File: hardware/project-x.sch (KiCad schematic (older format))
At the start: 14 parts

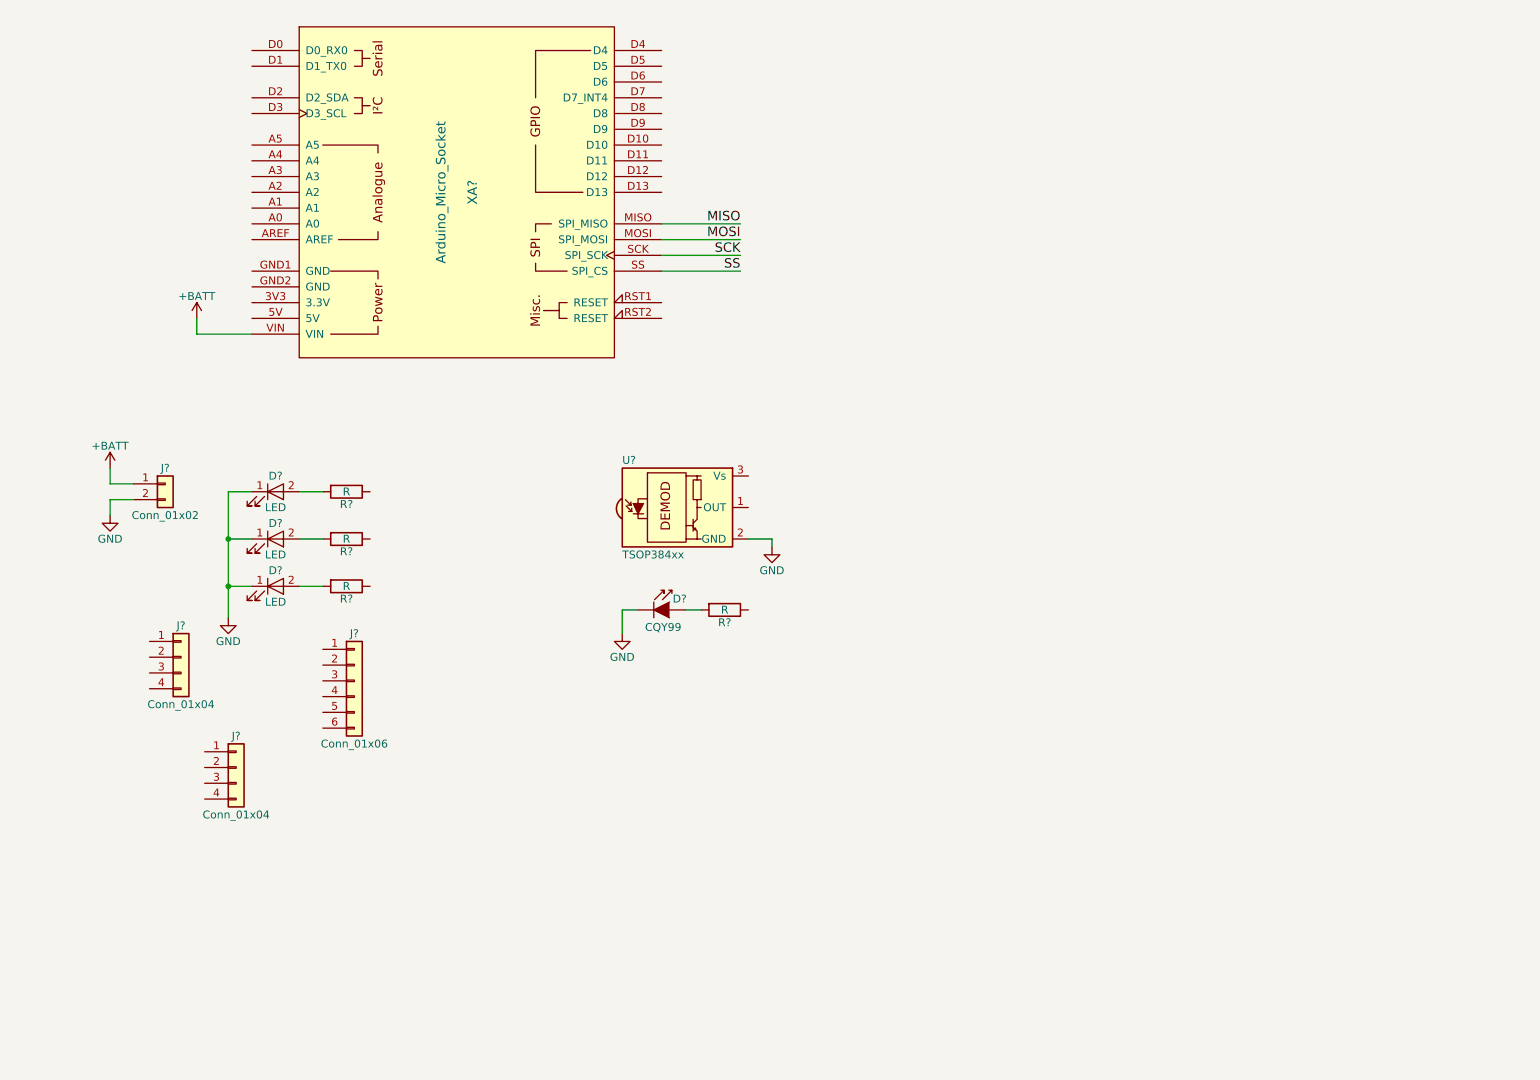
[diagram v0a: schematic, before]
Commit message: Add tags to schematic
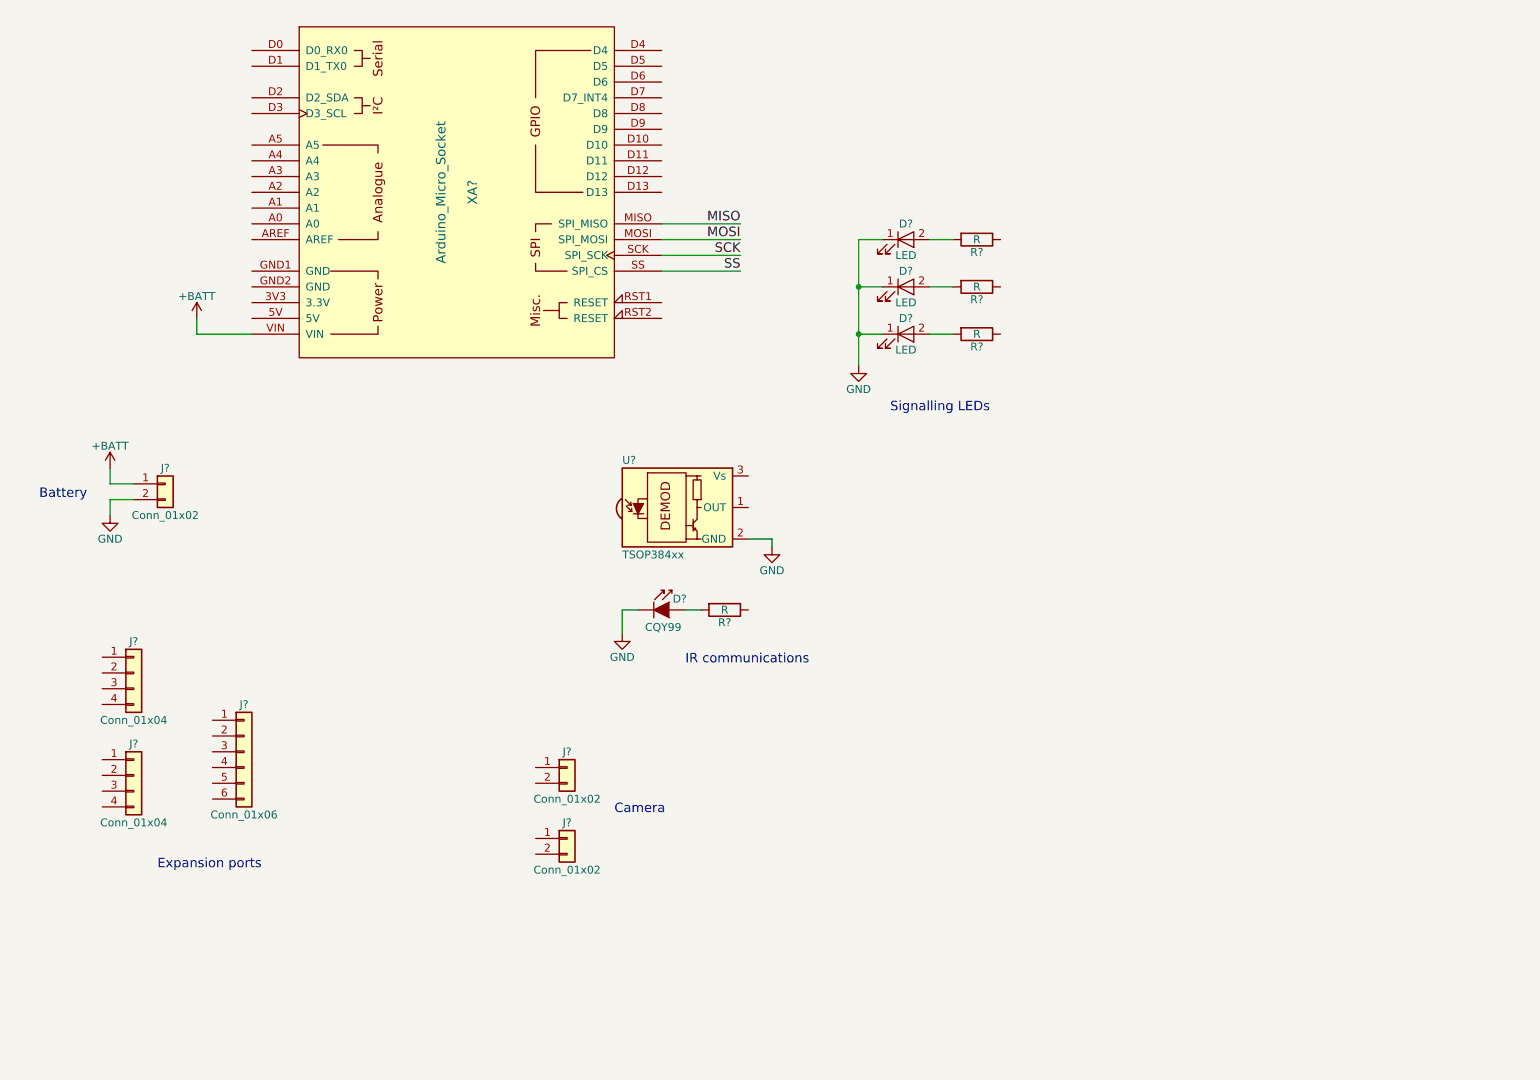
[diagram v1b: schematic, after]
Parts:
- added J? (x2): Conn_01x02, symbol Conn_01x02
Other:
- note added: "Battery"
- note added: "Camera"
- note added: "Expansion ports"
- note added: "IR communications"
- note added: "Signalling LEDs"
- moved on the sheet: D?, J?, R?
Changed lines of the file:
@@
 L LED D?
 U 1 1 5BD3A84D
-P 2200 4050
-F 0 "D?" H 2200 4150 50  0000 C CNN
-F 1 "LED" H 2200 3950 50  0000 C CNN
-F 2 "" H 2200 4050 50  0001 C CNN
-F 3 "" H 2200 4050 50  0001 C CNN
-	1    2200 4050
+P 6200 2450
+F 0 "D?" H 6200 2550 50  0000 C CNN
+F 1 "LED" H 6200 2350 50  0000 C CNN
+F 2 "" H 6200 2450 50  0001 C CNN
+F 3 "" H 6200 2450 50  0001 C CNN
+	1    6200 2450
 	1    0    0    -1
 $EndComp
@@
 L LED D?
 U 1 1 5BD3A889
-P 2200 4350
-F 0 "D?" H 2200 4450 50  0000 C CNN
-F 1 "LED" H 2200 4250 50  0000 C CNN
-F 2 "" H 2200 4350 50  0001 C CNN
-F 3 "" H 2200 4350 50  0001 C CNN
-	1    2200 4350
+P 6200 2750
+F 0 "D?" H 6200 2850 50  0000 C CNN
+F 1 "LED" H 6200 2650 50  0000 C CNN
+F 2 "" H 6200 2750 50  0001 C CNN
+F 3 "" H 6200 2750 50  0001 C CNN
+	1    6200 2750
 	1    0    0    -1
 $EndComp
@@
 L LED D?
 U 1 1 5BD3A8AF
-P 2200 4650
-F 0 "D?" H 2200 4750 50  0000 C CNN
-F 1 "LED" H 2200 4550 50  0000 C CNN
-F 2 "" H 2200 4650 50  0001 C CNN
-F 3 "" H 2200 4650 50  0001 C CNN
-	1    2200 4650
+P 6200 3050
+F 0 "D?" H 6200 3150 50  0000 C CNN
+F 1 "LED" H 6200 2950 50  0000 C CNN
+F 2 "" H 6200 3050 50  0001 C CNN
+F 3 "" H 6200 3050 50  0001 C CNN
+	1    6200 3050
 	1    0    0    -1
 $EndComp
@@
 L R R?
 U 1 1 5BD3A8D3
-P 2650 4050
-F 0 "R?" V 2730 4050 50  0000 C CNN
-F 1 "R" V 2650 4050 50  0000 C CNN
-F 2 "" V 2580 4050 50  0001 C CNN
-F 3 "" H 2650 4050 50  0001 C CNN
-	1    2650 4050
+P 6650 2450
+F 0 "R?" V 6730 2450 50  0000 C CNN
+F 1 "R" V 6650 2450 50  0000 C CNN
+F 2 "" V 6580 2450 50  0001 C CNN
+F 3 "" H 6650 2450 50  0001 C CNN
+	1    6650 2450
 	0    1    1    0
 $EndComp
@@
 L R R?
 U 1 1 5BD3A8F8
-P 2650 4350
-F 0 "R?" V 2730 4350 50  0000 C CNN
-F 1 "R" V 2650 4350 50  0000 C CNN
-F 2 "" V 2580 4350 50  0001 C CNN
-F 3 "" H 2650 4350 50  0001 C CNN
-	1    2650 4350
+P 6650 2750
+F 0 "R?" V 6730 2750 50  0000 C CNN
+F 1 "R" V 6650 2750 50  0000 C CNN
+F 2 "" V 6580 2750 50  0001 C CNN
+F 3 "" H 6650 2750 50  0001 C CNN
+	1    6650 2750
 	0    1    1    0
 $EndComp
@@
 L R R?
 U 1 1 5BD3A947
-P 2650 4650
-F 0 "R?" V 2730 4650 50  0000 C CNN
-F 1 "R" V 2650 4650 50  0000 C CNN
-F 2 "" V 2580 4650 50  0001 C CNN
-F 3 "" H 2650 4650 50  0001 C CNN
-	1    2650 4650
+P 6650 3050
+F 0 "R?" V 6730 3050 50  0000 C CNN
+F 1 "R" V 6650 3050 50  0000 C CNN
+F 2 "" V 6580 3050 50  0001 C CNN
+F 3 "" H 6650 3050 50  0001 C CNN
+	1    6650 3050
 	0    1    1    0
 $EndComp
@@
 L Conn_01x04 J?
 U 1 1 5BD3A97E
-P 1600 5100
-F 0 "J?" H 1600 5300 50  0000 C CNN
-F 1 "Conn_01x04" H 1600 4800 50  0000 C CNN
-F 2 "" H 1600 5100 50  0001 C CNN
-F 3 "" H 1600 5100 50  0001 C CNN
-	1    1600 5100
+P 1300 5200
+F 0 "J?" H 1300 5400 50  0000 C CNN
+F 1 "Conn_01x04" H 1300 4900 50  0000 C CNN
+F 2 "" H 1300 5200 50  0001 C CNN
+F 3 "" H 1300 5200 50  0001 C CNN
+	1    1300 5200
 	1    0    0    -1
 $EndComp
@@
 L Conn_01x04 J?
 U 1 1 5BD3AB10
-P 1950 5800
-F 0 "J?" H 1950 6000 50  0000 C CNN
-F 1 "Conn_01x04" H 1950 5500 50  0000 C CNN
-F 2 "" H 1950 5800 50  0001 C CNN
-F 3 "" H 1950 5800 50  0001 C CNN
-	1    1950 5800
+P 1300 5850
+F 0 "J?" H 1300 6050 50  0000 C CNN
+F 1 "Conn_01x04" H 1300 5550 50  0000 C CNN
+F 2 "" H 1300 5850 50  0001 C CNN
+F 3 "" H 1300 5850 50  0001 C CNN
+	1    1300 5850
 	1    0    0    -1
 $EndComp
@@
 L Conn_01x06 J?
 U 1 1 5BD3AB69
-P 2700 5250
-F 0 "J?" H 2700 5550 50  0000 C CNN
-F 1 "Conn_01x06" H 2700 4850 50  0000 C CNN
-F 2 "" H 2700 5250 50  0001 C CNN
-F 3 "" H 2700 5250 50  0001 C CNN
-	1    2700 5250
+P 2000 5700
+F 0 "J?" H 2000 6000 50  0000 C CNN
+F 1 "Conn_01x06" H 2000 5300 50  0000 C CNN
+F 2 "" H 2000 5700 50  0001 C CNN
+F 3 "" H 2000 5700 50  0001 C CNN
+	1    2000 5700
 	1    0    0    -1
 $EndComp
@@
 	4650 2650 5150 2650
 Wire Wire Line
-	2350 4050 2500 4050
-Wire Wire Line
-	2500 4350 2350 4350
-Wire Wire Line
-	2350 4650 2500 4650
-Wire Wire Line
-	2050 4050 1900 4050
-Wire Wire Line
-	1900 4050 1900 4850
-Wire Wire Line
-	2050 4650 1900 4650
-Connection ~ 1900 4650
-Wire Wire Line
-	2050 4350 1900 4350
-Connection ~ 1900 4350
+	6350 2450 6500 2450
+Wire Wire Line
+	6500 2750 6350 2750
+Wire Wire Line
+	6350 3050 6500 3050
+Wire Wire Line
+	6050 2450 5900 2450
+Wire Wire Line
+	5900 2450 5900 3250
+Wire Wire Line
+	6050 3050 5900 3050
+Connection ~ 5900 3050
+Wire Wire Line
+	6050 2750 5900 2750
+Connection ~ 5900 2750
 $Comp
 L GND #PWR?
 U 1 1 5BD452CA
-P 1900 4850
-F 0 "#PWR?" H 1900 4600 50  0001 C CNN
-F 1 "GND" H 1900 4700 50  0000 C CNN
-F 2 "" H 1900 4850 50  0001 C CNN
-F 3 "" H 1900 4850 50  0001 C CNN
-	1    1900 4850
+P 5900 3250
+F 0 "#PWR?" H 5900 3000 50  0001 C CNN
+F 1 "GND" H 5900 3100 50  0000 C CNN
+F 2 "" H 5900 3250 50  0001 C CNN
+F 3 "" H 5900 3250 50  0001 C CNN
+	1    5900 3250
 	1    0    0    -1
 $EndComp
@@
 Text Label 5150 2650 2    60   ~ 0
 SS
+$Comp
+L Conn_01x02 J?
+U 1 1 5BD45933
+P 4050 5800
+F 0 "J?" H 4050 5900 50  0000 C CNN
+F 1 "Conn_01x02" H 4050 5600 50  0000 C CNN
+F 2 "" H 4050 5800 50  0001 C CNN
+F 3 "" H 4050 5800 50  0001 C CNN
+	1    4050 5800
+	1    0    0    -1
+$EndComp
+$Comp
+L Conn_01x02 J?
+U 1 1 5BD45A35
+P 4050 6250
+F 0 "J?" H 4050 6350 50  0000 C CNN
+F 1 "Conn_01x02" H 4050 6050 50  0000 C CNN
+F 2 "" H 4050 6250 50  0001 C CNN
+F 3 "" H 4050 6250 50  0001 C CNN
+	1    4050 6250
+	1    0    0    -1
+$EndComp
+Text Notes 4350 6100 0    60   ~ 0
+Camera
+Text Notes 4800 5150 0    60   ~ 0
+IR communications
+Text Notes 700  4100 0    60   ~ 0
+Battery
+Text Notes 6100 3550 0    60   ~ 0
+Signalling LEDs
+Text Notes 1450 6450 0    60   ~ 0
+Expansion ports
 $EndSCHEMATC

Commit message: Add LEDs, connectors, button, IR, DC-DC
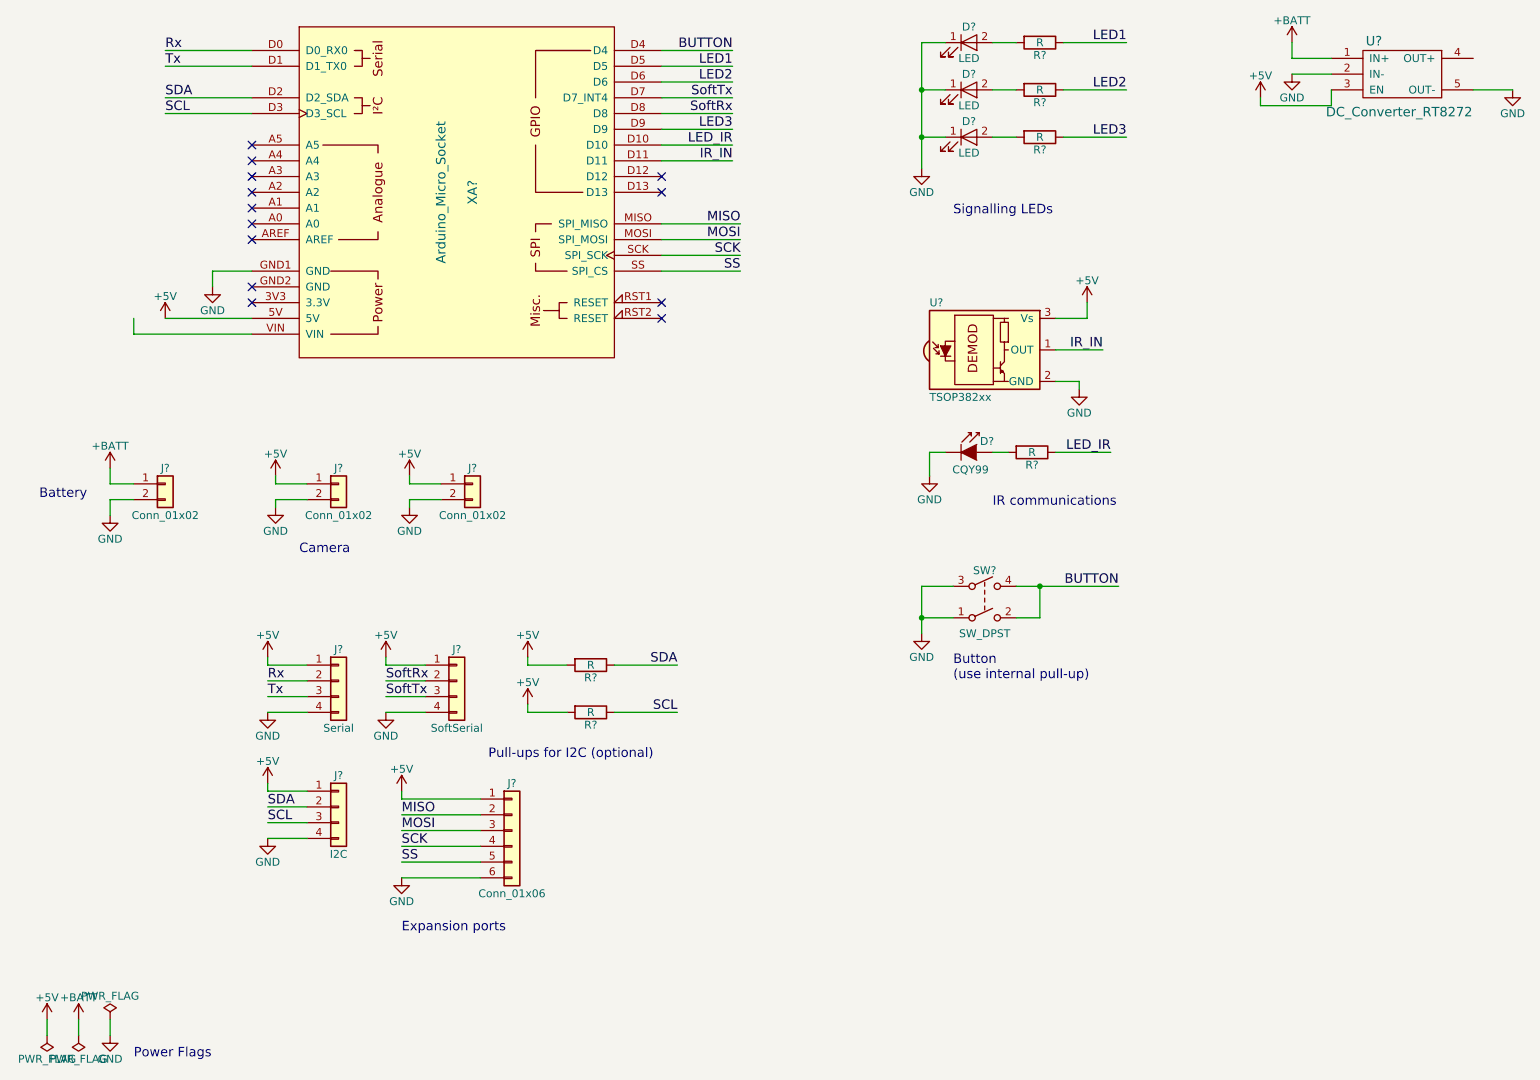
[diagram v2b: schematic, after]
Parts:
- removed J?: Conn_01x02, symbol Conn_01x02
- removed U?: TSOP384xx, Opto-Devices:IRReceiver_Vishay_MINICAST-3pin, symbol TSOP384xx
- added J?: SoftSerial, symbol Conn_01x04
- added J?: Conn_01x02, symbol Conn_01x02
- added R? (x2): R, symbol R
- added SW?: SW_DPST, symbol SW_DPST
- added U?: TSOP382xx, Opto-Devices:IRReceiver_Vishay_MINICAST-3pin, symbol TSOP382xx
- added U?: DC_Converter_RT8272, symbol DC_Converter_RT8272
- J?: value Conn_01x04 -> Serial
- J?: value Conn_01x04 -> I2C
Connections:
- net +BATT: now also U?.1 (IN+); no longer XA?.VIN
- net GND: now also J?.2 (Pin_2), J?.4 (Pin_4), J?.4 (Pin_4), J?.6 (Pin_6), XA?.GND1 (GND), J?.2 (Pin_2), J?.4 (Pin_4), SW?.1, SW?.3, U?.2 (GND), U?.2 (IN-), U?.5 (OUT-)
- net MISO: now also J?.2 (Pin_2)
- net MOSI: now also J?.3 (Pin_3)
- net SCK: now also J?.4 (Pin_4)
- net SS: now also J?.5 (Pin_5)
- net +5V: now reaches XA?.5V
- net +5V: now also J?.1 (Pin_1), J?.1 (Pin_1), J?.1 (Pin_1), J?.1 (Pin_1), J?.1 (Pin_1), J?.1 (Pin_1), R?.2, R?.2, U?.3 (EN), U?.3 (Vs)
- net Rx: now reaches XA?.D0 (D0_RX0)
- net Rx: now also J?.2 (Pin_2)
- net Tx: now reaches XA?.D1 (D1_TX0)
- net Tx: now also J?.3 (Pin_3)
- net LED_IR: now reaches XA?.D10
- net LED_IR: now also R?.1
- net IR_IN: now reaches XA?.D11
- net IR_IN: now also U?.1 (OUT)
- net SDA: now reaches XA?.D2 (D2_SDA)
- net SDA: now also J?.2 (Pin_2), R?.1
- net SCL: now reaches XA?.D3 (D3_SCL)
- net SCL: now also J?.3 (Pin_3), R?.1
- net BUTTON: now reaches XA?.D4
- net BUTTON: now also SW?.2, SW?.4
- net LED1: now reaches XA?.D5
- net LED1: now also R?.1
- net LED2: now reaches XA?.D6
- net LED2: now also R?.1
- net SoftTx: now reaches XA?.D7 (D7_INT4)
- net SoftTx: now also J?.3 (Pin_3)
- net SoftRx: now reaches XA?.D8
- net SoftRx: now also J?.2 (Pin_2)
- net LED3: now reaches XA?.D9
- net LED3: now also R?.1
- no-connect marks 0 -> 13
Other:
- note added: "Button \n(use internal pull-up)"
- note added: "Power Flags"
- note added: "Pull-ups for I2C (optional)\n"
- moved on the sheet: D?, J?, R?

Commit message: Fix connections
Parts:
- added J8: Conn_01x02, symbol Conn_01x02
- added JP1: Jumper_NO_Small, symbol Jumper_NO_Small
- gave numbers to parts that had none: 21
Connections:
- net +5V: now also JP1.1; no longer U2.3 (EN)
- net GND: now also J8.2 (Pin_2)
- net VCC: now reaches XA1.VIN
- net VCC: now also U2.4 (OUT+), J8.1 (Pin_1)
- new net: JP1.2, U2.3 (EN)
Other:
- note added: "Extra Power"
- note added: "RC Car"
- moved on the sheet: J2, J5, U1
